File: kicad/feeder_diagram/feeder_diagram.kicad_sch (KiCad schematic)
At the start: 72 parts, among them J1 USB_A, J2 ServoPort_01_kibble_tray, J3 ServoPort_02_Food_trap, SW1 CK_KMS2xxGP, U1 WEMOS_D1_mini, U2 HC-05_Bluetooth_Module

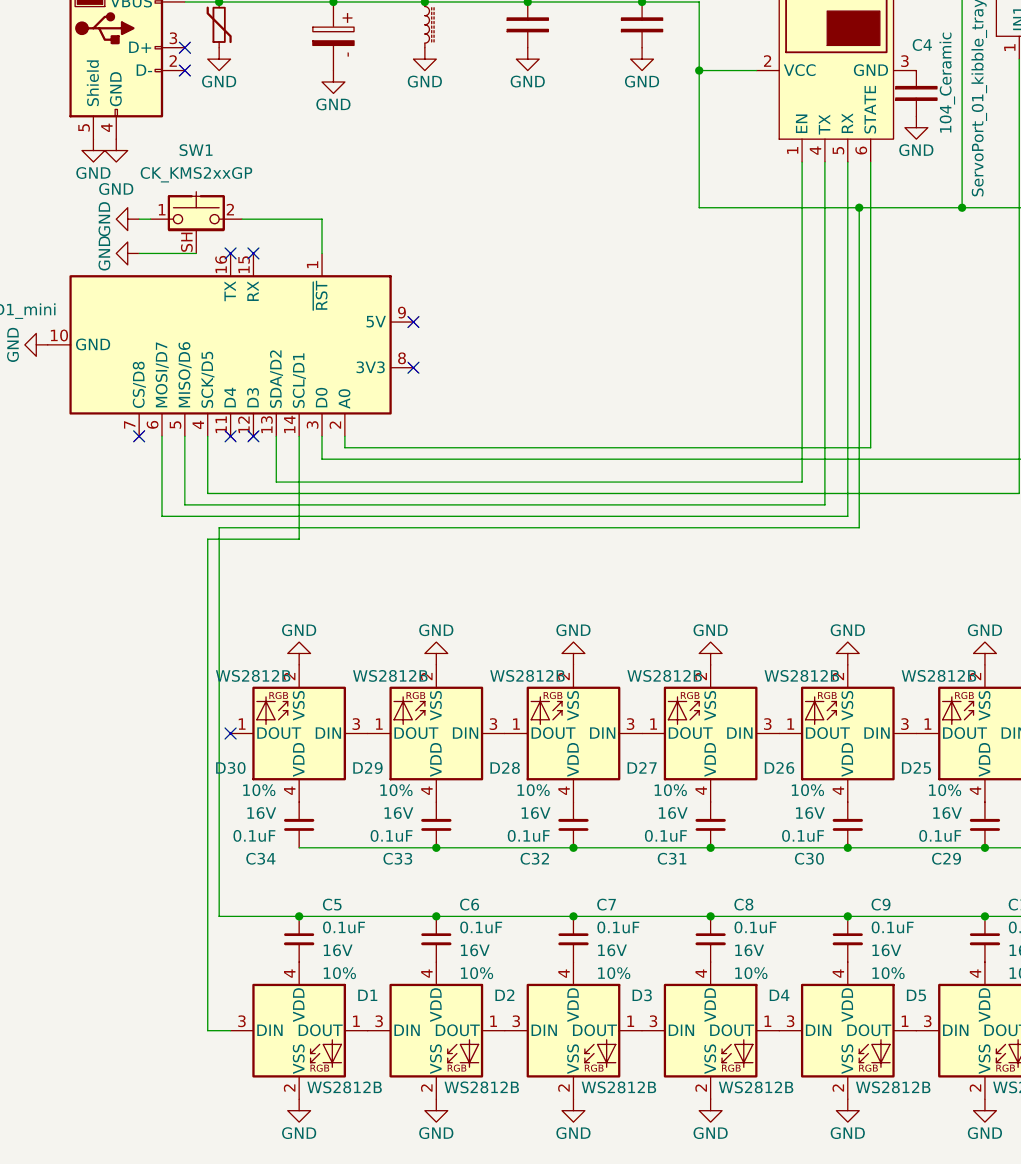
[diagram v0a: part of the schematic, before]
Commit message: [UPDATE] the food dispensing logic to be asynchronous
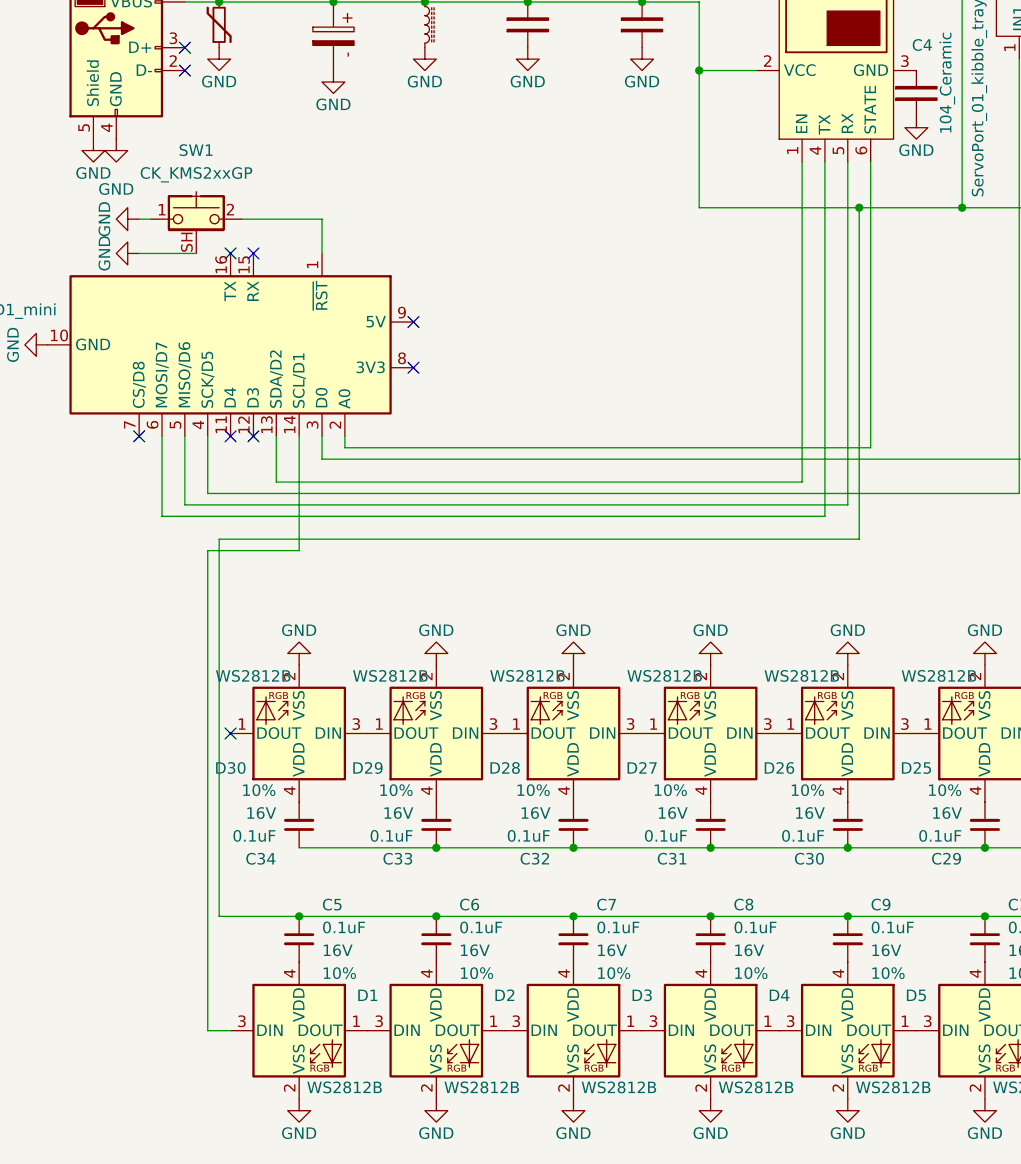
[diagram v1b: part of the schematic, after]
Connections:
- net at U1.5 (MISO/D6): now also U2.5 (RX); no longer U2.4 (TX)
- net at U1.6 (MOSI/D7): now also U2.4 (TX); no longer U2.5 (RX)
